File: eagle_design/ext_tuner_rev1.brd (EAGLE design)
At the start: 150.2 x 76.7 mm, 209 parts, among them J1 SMA0.062, J2 SMA0.062, J3 AMPHENOL_A-1JB, J4 SMA0.062, J5 1734035-2, J6 AMPHENOL_A-1JB, U1 PG-103+, U11 74ALS04D, U2 HMC636ST89ETR, U3 HMC636ST89ETR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

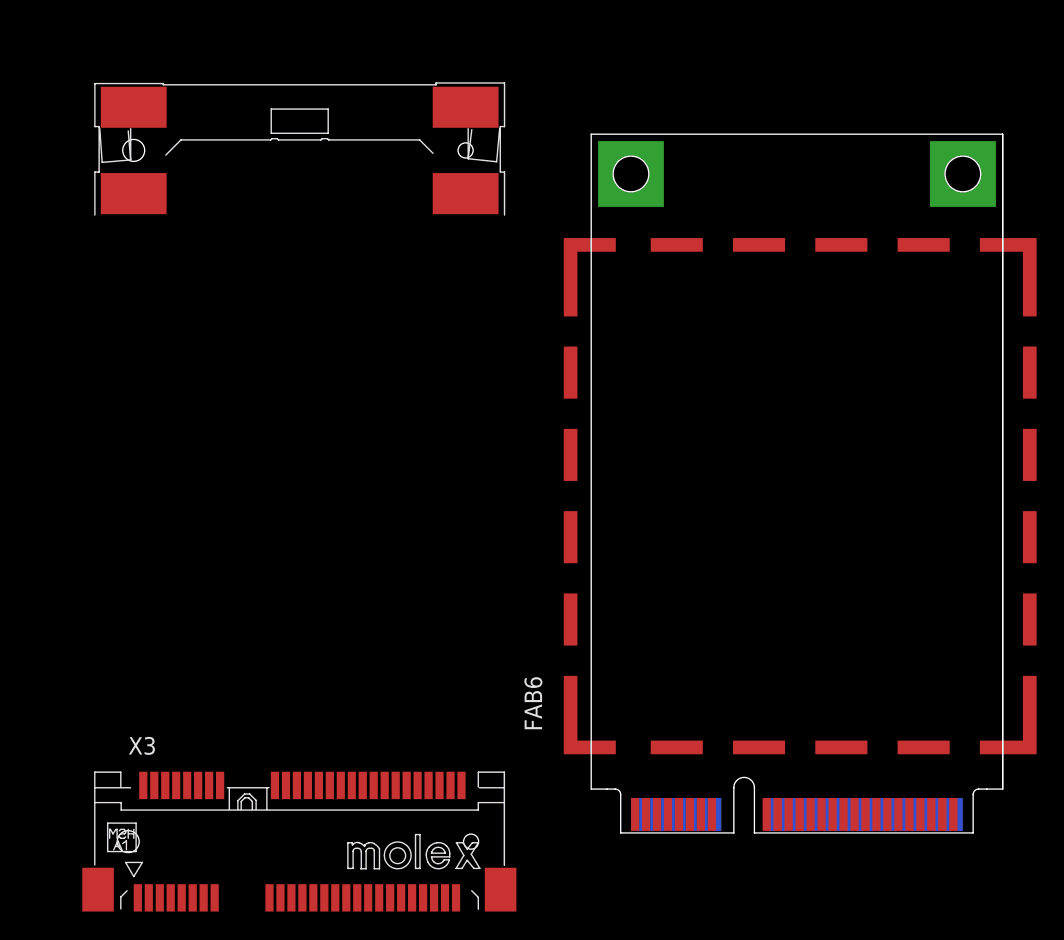
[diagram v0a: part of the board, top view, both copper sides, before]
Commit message: add ext tuner design
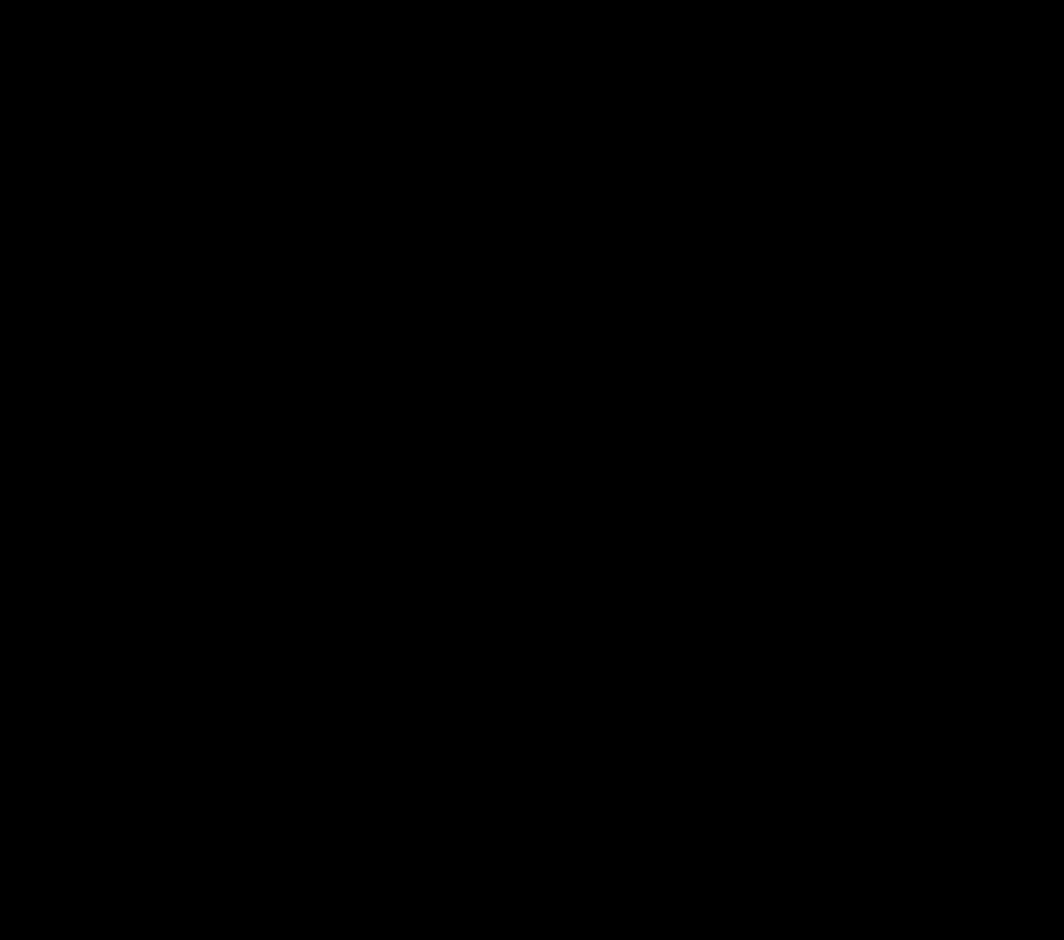
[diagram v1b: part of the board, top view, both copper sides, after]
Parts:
- removed FAB6: 2118724, rf_shield_pn_2118724:RF_SHIELD
- removed U$1: FULL-MINI-PCI-E, mini-pci-e:FULL-MINI-PCI-E
- removed X3: 679105700SMD, con-molex:679105700
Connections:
- net GND: no longer U$1.GND@1, U$1.GND@2
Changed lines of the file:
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@@
 <attribute name="NAME" x="41.5574" y="55.0408" size="0.8128" layer="25"/>
 </element>
-<element name="X3" library="con-molex" package="679105700" value="679105700SMD" x="164.6682" y="9.7536"/>
-<element name="U$1" library="mini-pci-e" package="FULL-MINI-PCI-E" value="FULL-MINI-PCI-E" x="209.5754" y="10.287"/>
-<element name="FAB6" library="rf_shield_pn_2118724" package="RF_SHIELD" value="2118724" x="213.8934" y="34.544" rot="R90"/>
 </elements>
 <signals>
@@
 <wire x1="105.804" y1="20.689" x2="106.9728" y2="20.689" width="0.254" layer="1"/>
 <wire x1="106.9728" y1="20.689" x2="107.0356" y2="20.7518" width="0.254" layer="1"/>
-<contactref element="U$1" pad="GND@1"/>
-<contactref element="U$1" pad="GND@2"/>
-<wire x1="201.3254" y1="58.437" x2="225.5254" y2="58.437" width="0" layer="19" extent="1-1"/>
-<wire x1="151.9936" y1="36.9062" x2="201.3254" y2="58.437" width="0" layer="19" extent="1-1"/>
 </signal>
 <signal name="N$17">
